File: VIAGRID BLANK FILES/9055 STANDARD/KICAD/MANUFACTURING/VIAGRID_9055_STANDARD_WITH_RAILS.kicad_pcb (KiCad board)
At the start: 2 copper layers, 100 x 65 mm, 0 parts

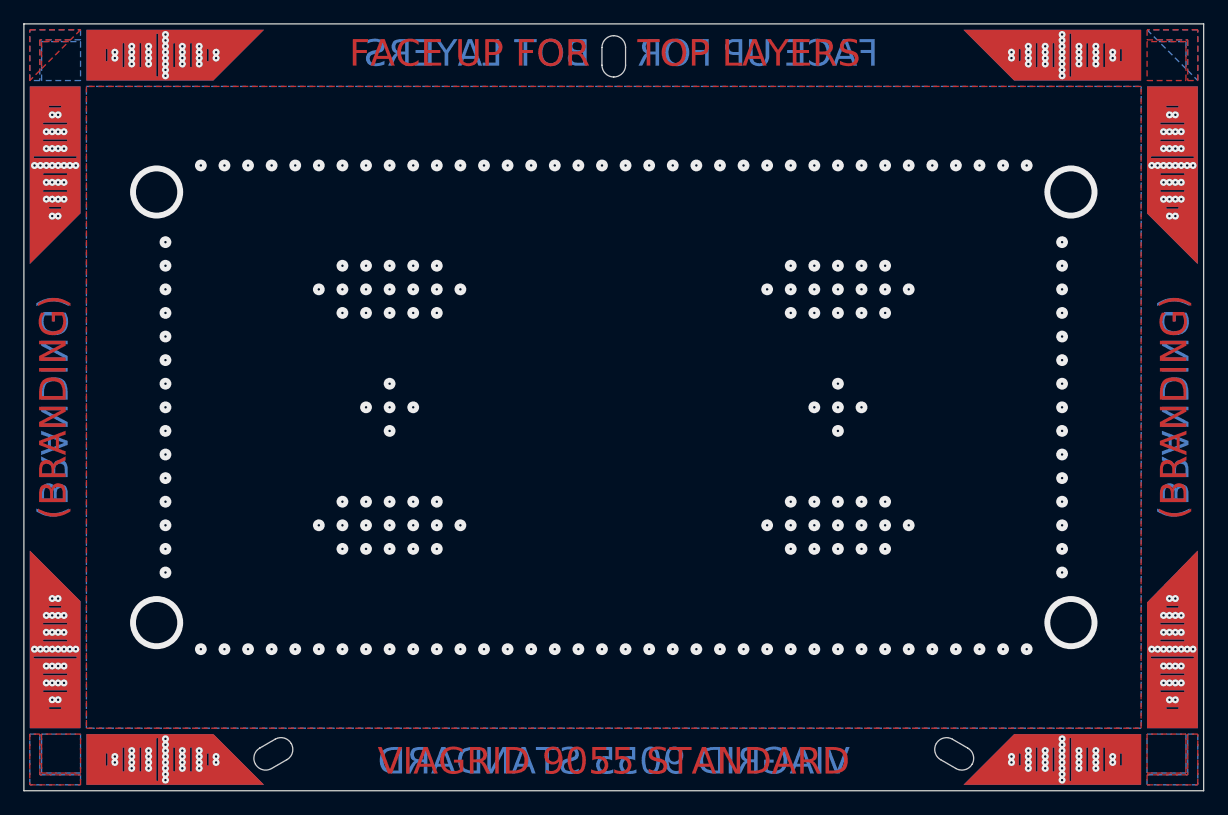
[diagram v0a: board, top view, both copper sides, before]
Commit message: feat(9055): replace (BRANDING) placeholder with SOCKEYE
The 9055 panel carried four "(BRANDING)" placeholder texts on the left
and right rails (F.Cu and B.Cu). The 6034 panel already reads SOCKEYE in
the same four positions; bring the 9055 in line.

Only the text string changes - position, rotation, layer and font are
untouched. The text sits on the rails outside the main GND pour, so no
zone refill is required.

Co-Authored-By: Claude Opus 5 (1M context) <noreply@anthropic.com>
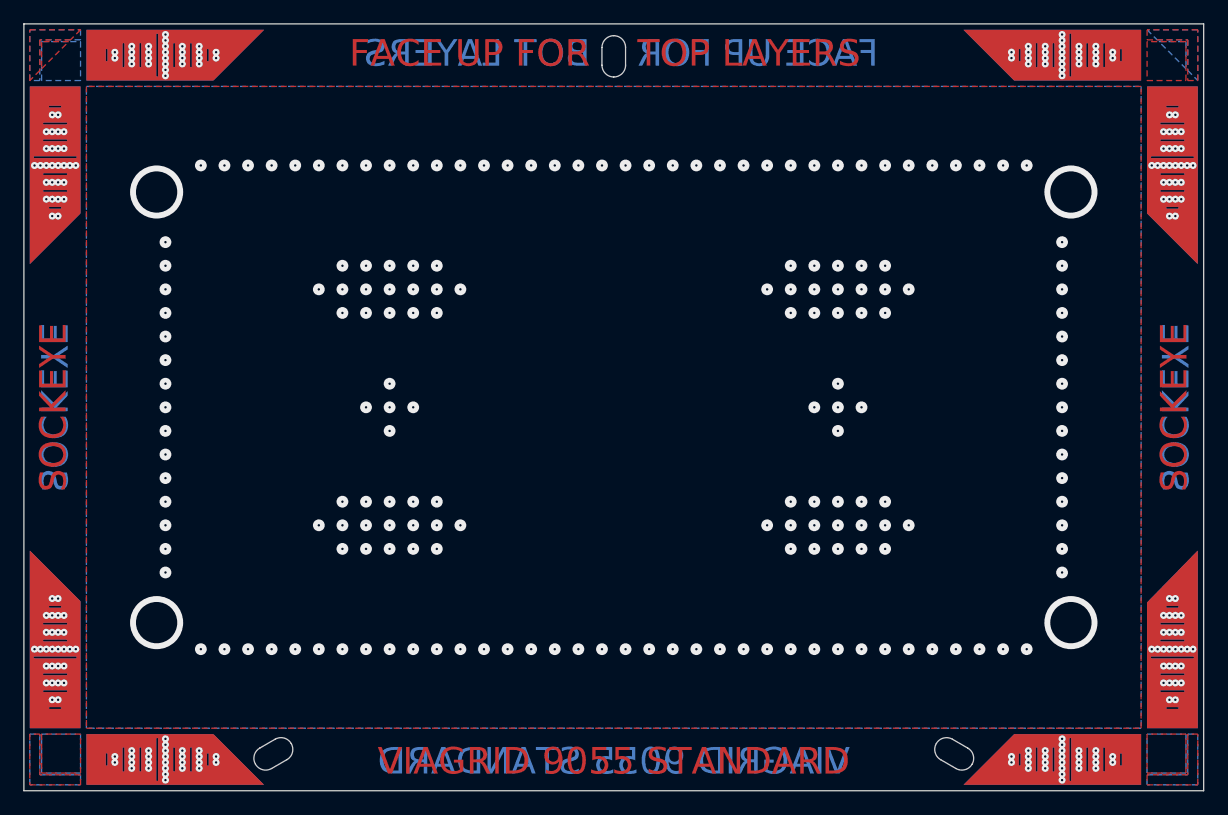
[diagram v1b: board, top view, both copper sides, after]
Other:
- board text added: "SOCKEYE"
- board text removed: "(BRANDING)"
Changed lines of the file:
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@@
 		(layer "User.1")
 	)
-	(gr_text "(BRANDING)"
+	(gr_text "SOCKEYE"
 		(at 196.25 88.75 90)
 		(layer "F.Cu")
@@
 		)
 	)
-	(gr_text "(BRANDING)"
+	(gr_text "SOCKEYE"
 		(at 101.25 88.75 90)
 		(layer "F.Cu")
@@
 		)
 	)
-	(gr_text "(BRANDING)"
+	(gr_text "SOCKEYE"
 		(at 101.25 88.75 270)
 		(layer "B.Cu")
@@
 		)
 	)
-	(gr_text "(BRANDING)"
+	(gr_text "SOCKEYE"
 		(at 196.25 88.75 270)
 		(layer "B.Cu")
